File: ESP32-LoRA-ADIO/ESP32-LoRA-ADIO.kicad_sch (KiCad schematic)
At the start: 30 parts, among them J1 USB_B_Micro, J2 External Power, J3 AIO/I2C, J4 DIO, J5 RXTX+Power, J6 SMA, J7 JTAG Debugging, Q1 IRLML5203, Q2 2N7002, Q3 2N7002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

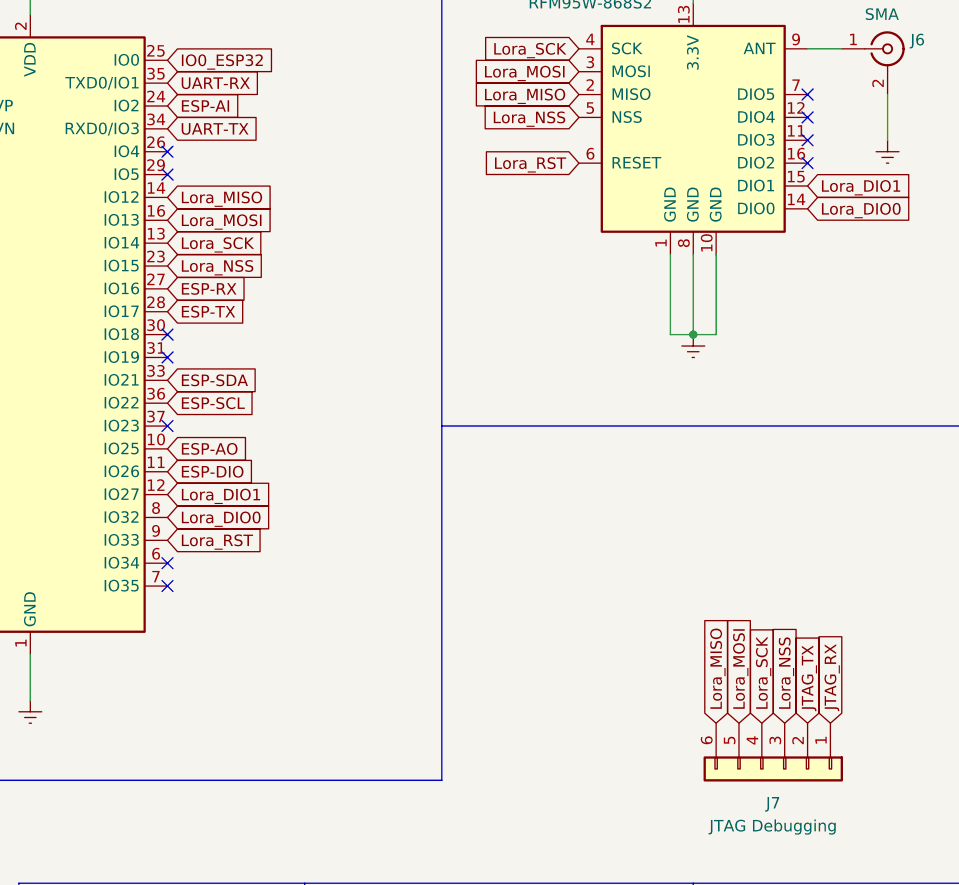
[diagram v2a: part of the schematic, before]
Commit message: Started to separate SPI and JTAG to be able to use both at the same time
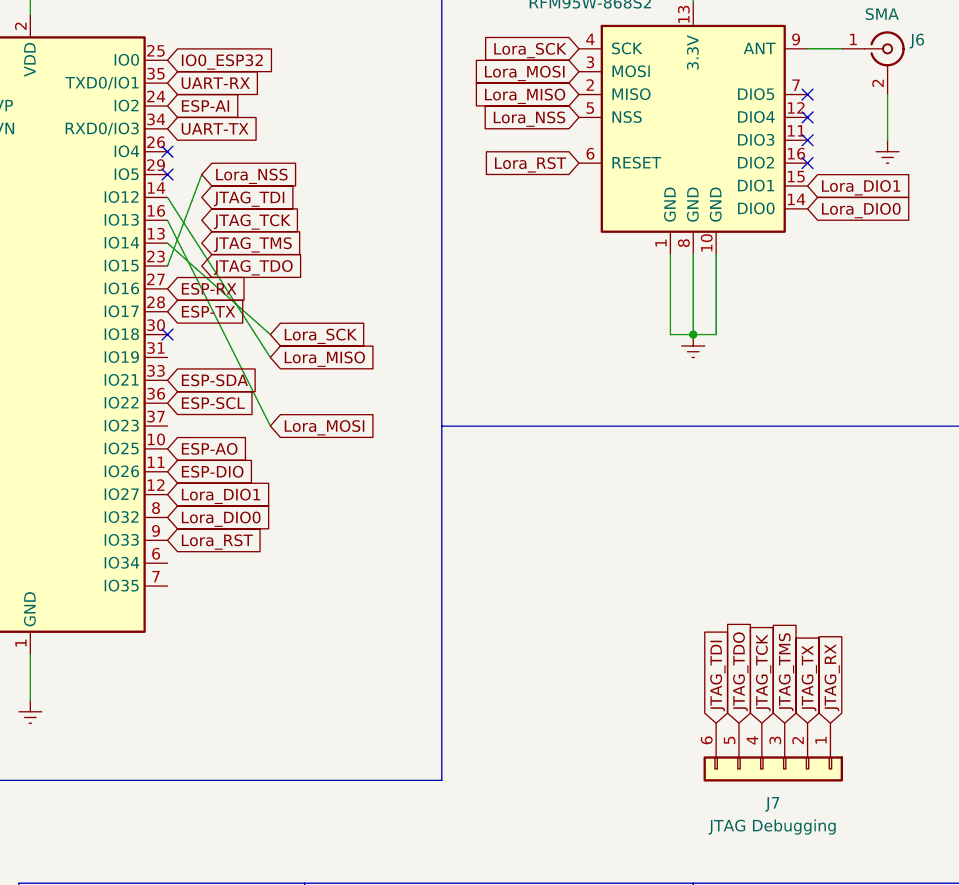
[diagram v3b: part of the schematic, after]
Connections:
- net Lora_MISO: no longer J7.6 (Pin_6)
- net Lora_MOSI: no longer J7.5 (Pin_5)
- net Lora_NSS: no longer J7.3 (Pin_3)
- net Lora_SCK: no longer J7.4 (Pin_4)
- new net JTAG_TCK: J7.4 (Pin_4)
- new net JTAG_TDI: J7.6 (Pin_6)
- new net JTAG_TDO: J7.5 (Pin_5)
- new net JTAG_TMS: J7.3 (Pin_3)
- no-connect marks 21 -> 17
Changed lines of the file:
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@@
   (no_connect (at 264.16 41.91))
   (no_connect (at 264.16 44.45))
-  (no_connect (at 193.04 73.66))
-  (no_connect (at 193.04 66.04))
   (no_connect (at 193.04 63.5))
   (no_connect (at 193.04 43.18))
   (no_connect (at 193.04 45.72))
-  (no_connect (at 193.04 91.44))
-  (no_connect (at 193.04 88.9))
   (wire (pts (xy 266.7 142.24) (xy 266.7 148.59))
     (stroke (width 0) (type default) (color 0 0 0 0))
@@
     (stroke (width 0) (type default) (color 0 0 0 0))
   )
+  (wire (pts (xy 204.47 63.5) (xy 193.04 53.34))
+    (stroke (width 0) (type default) (color 0 0 0 0))
+  )
   (wire (pts (xy 251.46 54.61) (xy 251.46 63.5))
     (stroke (width 0) (type default) (color 0 0 0 0))
@@
     (stroke (width 0) (type default) (color 0 0 0 0))
   )
+  (wire (pts (xy 204.47 73.66) (xy 193.04 50.8))
+    (stroke (width 0) (type default) (color 0 0 0 0))
+  )
   (wire (pts (xy 109.22 176.53) (xy 109.22 170.18))
     (stroke (width 0) (type default) (color 0 0 0 0))
@@
     (stroke (width 0) (type default) (color 0 0 0 0))
   )
+  (wire (pts (xy 196.85 45.72) (xy 193.04 55.88))
+    (stroke (width 0) (type default) (color 0 0 0 0))
+  )
   (wire (pts (xy 78.74 176.53) (xy 83.82 176.53))
     (stroke (width 0) (type default) (color 0 0 0 0))
@@
     (stroke (width 0) (type default) (color 0 0 0 0))
   )
+  (wire (pts (xy 204.47 66.04) (xy 193.04 48.26))
+    (stroke (width 0) (type default) (color 0 0 0 0))
+  )
   (wire (pts (xy 193.04 138.43) (xy 193.04 153.67))
     (stroke (width 0) (type default) (color 0 0 0 0))
@@
     )
   )
+  (global_label "JTAG_TDO" (shape input) (at 196.85 55.88 0) (fields_autoplaced)
+    (effects (font (size 1.27 1.27)) (justify left))
+    (property "Intersheet References" "${INTERSHEET_REFS}" (id 0) (at 208.0037 55.8006 0)
+      (effects (font (size 1.27 1.27)) (justify left) hide)
+    )
+  )
+  (global_label "JTAG_TMS" (shape input) (at 261.62 106.68 90) (fields_autoplaced)
+    (effects (font (size 1.27 1.27)) (justify left))
+    (property "Intersheet References" "${INTERSHEET_REFS}" (id 0) (at 261.5406 95.4658 90)
+      (effects (font (size 1.27 1.27)) (justify left) hide)
+    )
+  )
+  (global_label "JTAG_TCK" (shape input) (at 196.85 50.8 0) (fields_autoplaced)
+    (effects (font (size 1.27 1.27)) (justify left))
+    (property "Intersheet References" "${INTERSHEET_REFS}" (id 0) (at 207.9432 50.7206 0)
+      (effects (font (size 1.27 1.27)) (justify left) hide)
+    )
+  )
   (global_label "IO0_ESP32" (shape input) (at 120.65 78.74 0) (fields_autoplaced)
     (effects (font (size 1.27 1.27)) (justify left))
@@
     )
   )
-  (global_label "Lora_SCK" (shape input) (at 193.04 53.34 0) (fields_autoplaced)
+  (global_label "Lora_SCK" (shape input) (at 204.47 63.5 0) (fields_autoplaced)
     (effects (font (size 1.27 1.27)) (justify left))
-    (property "Intersheet References" "${INTERSHEET_REFS}" (id 0) (at 17.78 -6.35 0)
+    (property "Intersheet References" "${INTERSHEET_REFS}" (id 0) (at 29.21 3.81 0)
       (effects (font (size 1.27 1.27)) hide)
     )
@@
     )
   )
-  (global_label "Lora_MISO" (shape input) (at 254 106.68 90) (fields_autoplaced)
-    (effects (font (size 1.27 1.27)) (justify left))
-    (property "Intersheet References" "${INTERSHEET_REFS}" (id 0) (at 199.39 281.94 0)
-      (effects (font (size 1.27 1.27)) hide)
-    )
-  )
   (global_label "ESP-AO" (shape input) (at 193.04 76.2 0) (fields_autoplaced)
     (effects (font (size 1.27 1.27)) (justify left))
@@
     )
   )
+  (global_label "JTAG_TX" (shape input) (at 264.16 106.68 90) (fields_autoplaced)
+    (effects (font (size 1.27 1.27)) (justify left))
+    (property "Intersheet References" "${INTERSHEET_REFS}" (id 0) (at 264.0806 96.9172 90)
+      (effects (font (size 1.27 1.27)) (justify left) hide)
+    )
+  )
   (global_label "DTR" (shape input) (at 120.65 53.34 0) (fields_autoplaced)
     (effects (font (size 1.27 1.27)) (justify left))
@@
     )
   )
-  (global_label "Lora_MOSI" (shape input) (at 256.54 106.68 90) (fields_autoplaced)
-    (effects (font (size 1.27 1.27)) (justify left))
-    (property "Intersheet References" "${INTERSHEET_REFS}" (id 0) (at 199.39 281.94 0)
-      (effects (font (size 1.27 1.27)) hide)
-    )
-  )
   (global_label "ESP-TX" (shape input) (at 274.32 143.51 90) (fields_autoplaced)
     (effects (font (size 1.27 1.27)) (justify left))
@@
     )
   )
-  (global_label "Lora_NSS" (shape input) (at 261.62 106.68 90) (fields_autoplaced)
+  (global_label "JTAG_TDI" (shape input) (at 254 106.68 90) (fields_autoplaced)
     (effects (font (size 1.27 1.27)) (justify left))
-    (property "Intersheet References" "${INTERSHEET_REFS}" (id 0) (at 199.39 281.94 0)
-      (effects (font (size 1.27 1.27)) hide)
+    (property "Intersheet References" "${INTERSHEET_REFS}" (id 0) (at 253.9206 96.252 90)
+      (effects (font (size 1.27 1.27)) (justify left) hide)
+    )
+  )
+  (global_label "JTAG_TDO" (shape input) (at 256.54 106.68 90) (fields_autoplaced)
+    (effects (font (size 1.27 1.27)) (justify left))
+    (property "Intersheet References" "${INTERSHEET_REFS}" (id 0) (at 256.4606 95.5263 90)
+      (effects (font (size 1.27 1.27)) (justify left) hide)
     )
   )
@@
     )
   )
-  (global_label "JTAG_TX" (shape input) (at 264.16 106.68 90) (fields_autoplaced)
-    (effects (font (size 1.27 1.27)) (justify left))
-    (property "Intersheet References" "${INTERSHEET_REFS}" (id 0) (at 264.0806 96.9172 90)
-      (effects (font (size 1.27 1.27)) (justify left) hide)
-    )
-  )
   (global_label "DTR" (shape input) (at 95.25 95.25 180) (fields_autoplaced)
     (effects (font (size 1.27 1.27)) (justify right))
@@
     )
   )
-  (global_label "JTAG_RX" (shape input) (at 266.7 106.68 90) (fields_autoplaced)
-    (effects (font (size 1.27 1.27)) (justify left))
-    (property "Intersheet References" "${INTERSHEET_REFS}" (id 0) (at 266.6206 96.6148 90)
-      (effects (font (size 1.27 1.27)) (justify left) hide)
-    )
-  )
   (global_label "ESP-RX" (shape input) (at 271.78 143.51 90) (fields_autoplaced)
     (effects (font (size 1.27 1.27)) (justify left))
@@
     )
   )
-  (global_label "Lora_MOSI" (shape input) (at 193.04 50.8 0) (fields_autoplaced)
+  (global_label "Lora_MOSI" (shape input) (at 204.47 73.66 0) (fields_autoplaced)
     (effects (font (size 1.27 1.27)) (justify left))
-    (property "Intersheet References" "${INTERSHEET_REFS}" (id 0) (at 17.78 -6.35 0)
+    (property "Intersheet References" "${INTERSHEET_REFS}" (id 0) (at 29.21 16.51 0)
       (effects (font (size 1.27 1.27)) hide)
     )
@@
     )
   )
+  (global_label "JTAG_TDI" (shape input) (at 196.85 48.26 0) (fields_autoplaced)
+    (effects (font (size 1.27 1.27)) (justify left))
+    (property "Intersheet References" "${INTERSHEET_REFS}" (id 0) (at 207.278 48.1806 0)
+      (effects (font (size 1.27 1.27)) (justify left) hide)
+    )
+  )
   (global_label "JTAG_RX" (shape input) (at 162.56 68.58 180) (fields_autoplaced)
     (effects (font (size 1.27 1.27)) (justify right))
@@
     )
   )
-  (global_label "Lora_MISO" (shape input) (at 193.04 48.26 0) (fields_autoplaced)
+  (global_label "Lora_MISO" (shape input) (at 204.47 66.04 0) (fields_autoplaced)
     (effects (font (size 1.27 1.27)) (justify left))
-    (property "Intersheet References" "${INTERSHEET_REFS}" (id 0) (at 17.78 -6.35 0)
+    (property "Intersheet References" "${INTERSHEET_REFS}" (id 0) (at 29.21 11.43 0)
       (effects (font (size 1.27 1.27)) hide)
     )
@@
     )
   )
+  (global_label "JTAG_TCK" (shape input) (at 259.08 106.68 90) (fields_autoplaced)
+    (effects (font (size 1.27 1.27)) (justify left))
+    (property "Intersheet References" "${INTERSHEET_REFS}" (id 0) (at 259.0006 95.5868 90)
+      (effects (font (size 1.27 1.27)) (justify left) hide)
+    )
+  )
   (global_label "RTS" (shape input) (at 95.25 91.44 180) (fields_autoplaced)
     (effects (font (size 1.27 1.27)) (justify right))
@@
     )
   )
-  (global_label "Lora_NSS" (shape input) (at 193.04 55.88 0) (fields_autoplaced)
+  (global_label "Lora_NSS" (shape input) (at 196.85 45.72 0) (fields_autoplaced)
     (effects (font (size 1.27 1.27)) (justify left))
-    (property "Intersheet References" "${INTERSHEET_REFS}" (id 0) (at 17.78 -6.35 0)
+    (property "Intersheet References" "${INTERSHEET_REFS}" (id 0) (at 21.59 -16.51 0)
       (effects (font (size 1.27 1.27)) hide)
     )
   )
-  (global_label "Lora_SCK" (shape input) (at 259.08 106.68 90) (fields_autoplaced)
+  (global_label "JTAG_RX" (shape input) (at 266.7 106.68 90) (fields_autoplaced)
     (effects (font (size 1.27 1.27)) (justify left))
-    (property "Intersheet References" "${INTERSHEET_REFS}" (id 0) (at 199.39 281.94 0)
-      (effects (font (size 1.27 1.27)) hide)
+    (property "Intersheet References" "${INTERSHEET_REFS}" (id 0) (at 266.6206 96.6148 90)
+      (effects (font (size 1.27 1.27)) (justify left) hide)
+    )
+  )
+  (global_label "JTAG_TMS" (shape input) (at 196.85 53.34 0) (fields_autoplaced)
+    (effects (font (size 1.27 1.27)) (justify left))
+    (property "Intersheet References" "${INTERSHEET_REFS}" (id 0) (at 208.0642 53.2606 0)
+      (effects (font (size 1.27 1.27)) (justify left) hide)
     )
   )

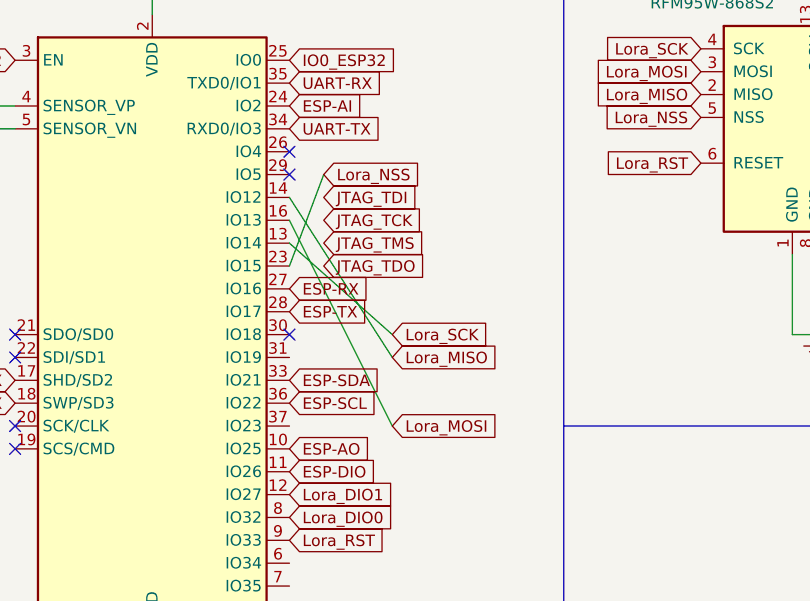
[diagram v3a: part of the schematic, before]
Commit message: Finalized the labeling - now the PCB needs to be changed
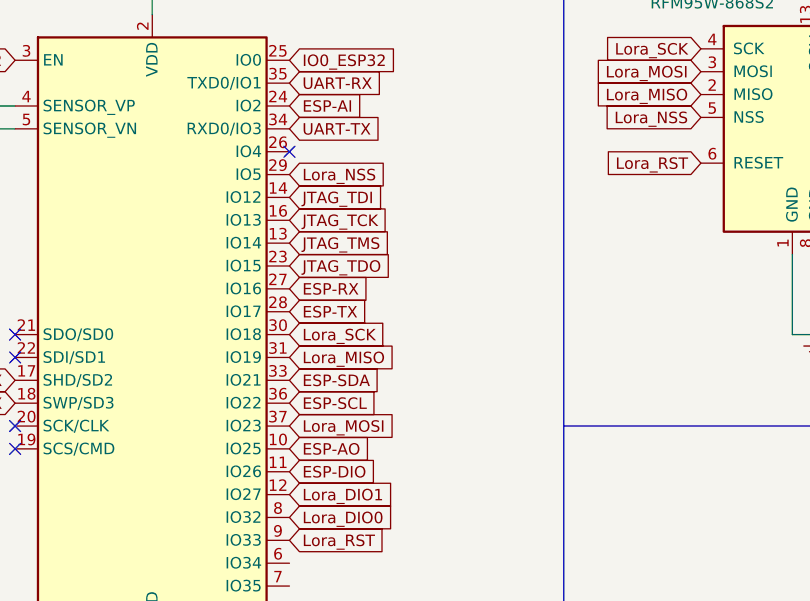
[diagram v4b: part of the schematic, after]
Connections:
- net JTAG_TCK: now also U3.16 (IO13)
- net JTAG_TDI: now also U3.14 (IO12)
- net JTAG_TDO: now also U3.23 (IO15)
- net JTAG_TMS: now also U3.13 (IO14)
- net Lora_MISO: now also U3.31 (IO19); no longer U3.14 (IO12)
- net Lora_MOSI: now also U3.37 (IO23); no longer U3.16 (IO13)
- net Lora_NSS: now also U3.29 (IO5); no longer U3.23 (IO15)
- net Lora_SCK: now also U3.30 (IO18); no longer U3.13 (IO14)
- no-connect marks 17 -> 15
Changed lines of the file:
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@@
   (no_connect (at 264.16 41.91))
   (no_connect (at 264.16 44.45))
-  (no_connect (at 193.04 63.5))
   (no_connect (at 193.04 43.18))
-  (no_connect (at 193.04 45.72))
   (wire (pts (xy 266.7 142.24) (xy 266.7 148.59))
     (stroke (width 0) (type default) (color 0 0 0 0))
@@
     (stroke (width 0) (type default) (color 0 0 0 0))
   )
-  (wire (pts (xy 204.47 63.5) (xy 193.04 53.34))
-    (stroke (width 0) (type default) (color 0 0 0 0))
-  )
   (wire (pts (xy 251.46 54.61) (xy 251.46 63.5))
     (stroke (width 0) (type default) (color 0 0 0 0))
@@
     (stroke (width 0) (type default) (color 0 0 0 0))
   )
-  (wire (pts (xy 204.47 73.66) (xy 193.04 50.8))
-    (stroke (width 0) (type default) (color 0 0 0 0))
-  )
   (wire (pts (xy 109.22 176.53) (xy 109.22 170.18))
     (stroke (width 0) (type default) (color 0 0 0 0))
@@
     (stroke (width 0) (type default) (color 0 0 0 0))
   )
-  (wire (pts (xy 196.85 45.72) (xy 193.04 55.88))
-    (stroke (width 0) (type default) (color 0 0 0 0))
-  )
   (wire (pts (xy 78.74 176.53) (xy 83.82 176.53))
     (stroke (width 0) (type default) (color 0 0 0 0))
@@
     (stroke (width 0) (type default) (color 0 0 0 0))
   )
-  (wire (pts (xy 204.47 66.04) (xy 193.04 48.26))
-    (stroke (width 0) (type default) (color 0 0 0 0))
-  )
   (wire (pts (xy 193.04 138.43) (xy 193.04 153.67))
     (stroke (width 0) (type default) (color 0 0 0 0))
@@
     )
   )
-  (global_label "JTAG_TDO" (shape input) (at 196.85 55.88 0) (fields_autoplaced)
+  (global_label "JTAG_TDO" (shape input) (at 193.04 55.88 0) (fields_autoplaced)
     (effects (font (size 1.27 1.27)) (justify left))
-    (property "Intersheet References" "${INTERSHEET_REFS}" (id 0) (at 208.0037 55.8006 0)
+    (property "Intersheet References" "${INTERSHEET_REFS}" (id 0) (at 204.1937 55.8006 0)
       (effects (font (size 1.27 1.27)) (justify left) hide)
     )
@@
     )
   )
-  (global_label "JTAG_TCK" (shape input) (at 196.85 50.8 0) (fields_autoplaced)
+  (global_label "JTAG_TCK" (shape input) (at 193.04 50.8 0) (fields_autoplaced)
     (effects (font (size 1.27 1.27)) (justify left))
-    (property "Intersheet References" "${INTERSHEET_REFS}" (id 0) (at 207.9432 50.7206 0)
+    (property "Intersheet References" "${INTERSHEET_REFS}" (id 0) (at 204.1332 50.7206 0)
       (effects (font (size 1.27 1.27)) (justify left) hide)
     )
@@
     )
   )
-  (global_label "Lora_SCK" (shape input) (at 204.47 63.5 0) (fields_autoplaced)
+  (global_label "Lora_SCK" (shape input) (at 193.04 63.5 0) (fields_autoplaced)
     (effects (font (size 1.27 1.27)) (justify left))
-    (property "Intersheet References" "${INTERSHEET_REFS}" (id 0) (at 29.21 3.81 0)
+    (property "Intersheet References" "${INTERSHEET_REFS}" (id 0) (at 17.78 3.81 0)
       (effects (font (size 1.27 1.27)) hide)
     )
@@
     )
   )
-  (global_label "Lora_MOSI" (shape input) (at 204.47 73.66 0) (fields_autoplaced)
+  (global_label "Lora_MOSI" (shape input) (at 193.04 73.66 0) (fields_autoplaced)
     (effects (font (size 1.27 1.27)) (justify left))
-    (property "Intersheet References" "${INTERSHEET_REFS}" (id 0) (at 29.21 16.51 0)
+    (property "Intersheet References" "${INTERSHEET_REFS}" (id 0) (at 17.78 16.51 0)
       (effects (font (size 1.27 1.27)) hide)
     )
@@
     )
   )
-  (global_label "JTAG_TDI" (shape input) (at 196.85 48.26 0) (fields_autoplaced)
+  (global_label "JTAG_TDI" (shape input) (at 193.04 48.26 0) (fields_autoplaced)
     (effects (font (size 1.27 1.27)) (justify left))
-    (property "Intersheet References" "${INTERSHEET_REFS}" (id 0) (at 207.278 48.1806 0)
+    (property "Intersheet References" "${INTERSHEET_REFS}" (id 0) (at 203.468 48.1806 0)
       (effects (font (size 1.27 1.27)) (justify left) hide)
     )
@@
     )
   )
-  (global_label "Lora_MISO" (shape input) (at 204.47 66.04 0) (fields_autoplaced)
+  (global_label "Lora_MISO" (shape input) (at 193.04 66.04 0) (fields_autoplaced)
     (effects (font (size 1.27 1.27)) (justify left))
-    (property "Intersheet References" "${INTERSHEET_REFS}" (id 0) (at 29.21 11.43 0)
+    (property "Intersheet References" "${INTERSHEET_REFS}" (id 0) (at 17.78 11.43 0)
       (effects (font (size 1.27 1.27)) hide)
     )
@@
     )
   )
-  (global_label "Lora_NSS" (shape input) (at 196.85 45.72 0) (fields_autoplaced)
+  (global_label "Lora_NSS" (shape input) (at 193.04 45.72 0) (fields_autoplaced)
     (effects (font (size 1.27 1.27)) (justify left))
-    (property "Intersheet References" "${INTERSHEET_REFS}" (id 0) (at 21.59 -16.51 0)
+    (property "Intersheet References" "${INTERSHEET_REFS}" (id 0) (at 17.78 -16.51 0)
       (effects (font (size 1.27 1.27)) hide)
     )
@@
     )
   )
-  (global_label "JTAG_TMS" (shape input) (at 196.85 53.34 0) (fields_autoplaced)
+  (global_label "JTAG_TMS" (shape input) (at 193.04 53.34 0) (fields_autoplaced)
     (effects (font (size 1.27 1.27)) (justify left))
-    (property "Intersheet References" "${INTERSHEET_REFS}" (id 0) (at 208.0642 53.2606 0)
+    (property "Intersheet References" "${INTERSHEET_REFS}" (id 0) (at 204.2542 53.2606 0)
       (effects (font (size 1.27 1.27)) (justify left) hide)
     )
